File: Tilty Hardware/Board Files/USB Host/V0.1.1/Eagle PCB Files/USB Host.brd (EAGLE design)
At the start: 38.1 x 50.8 mm, 24 parts, among them U1 MAX3421E, U2 AP7313SOT23R, U3 LM2931

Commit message: A bunch of changes to things.todo after assembling new prototypes
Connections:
- removed net N$27: JP4.P$6
- net INT: now also JP4.P$6
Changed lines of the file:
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@@
 <contactref element="JP4" pad="P$5"/>
-</signal>
-<signal name="N$27">
-<contactref element="JP4" pad="P$6"/>
 </signal>
 <signal name="3V_SCL">
@@
 <wire x1="17.8" y1="18.744" x2="17.8" y2="17.1495" width="0.2032" layer="1"/>
 <wire x1="17.8" y1="17.1495" x2="17.8045" y2="17.145" width="0.2032" layer="1"/>
+<contactref element="JP4" pad="P$6"/>
+<wire x1="17.8" y1="18.744" x2="30.607" y2="36.703" width="0" layer="19" extent="1-1"/>
 </signal>
 <signal name="RST">

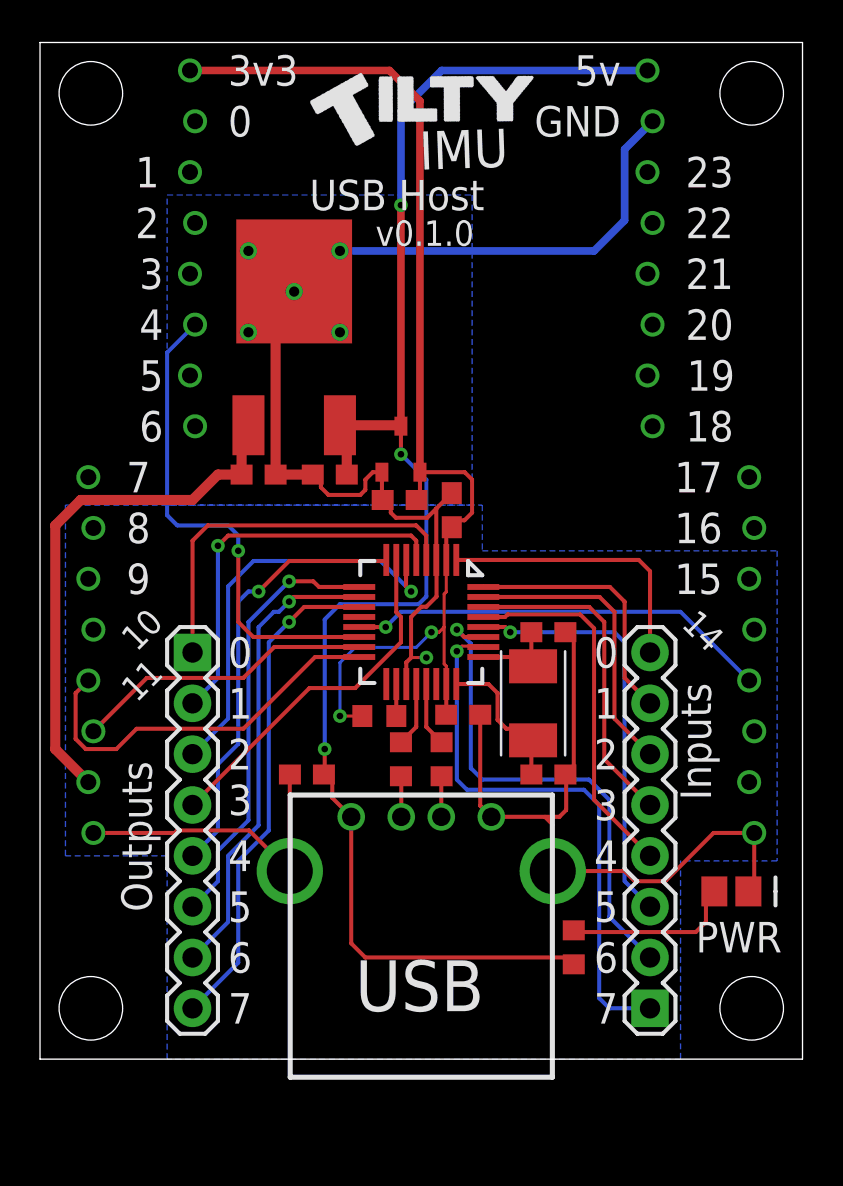
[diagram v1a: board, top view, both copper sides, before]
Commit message: Added Tilty silkscreen and option 5/3.3v I2C connections
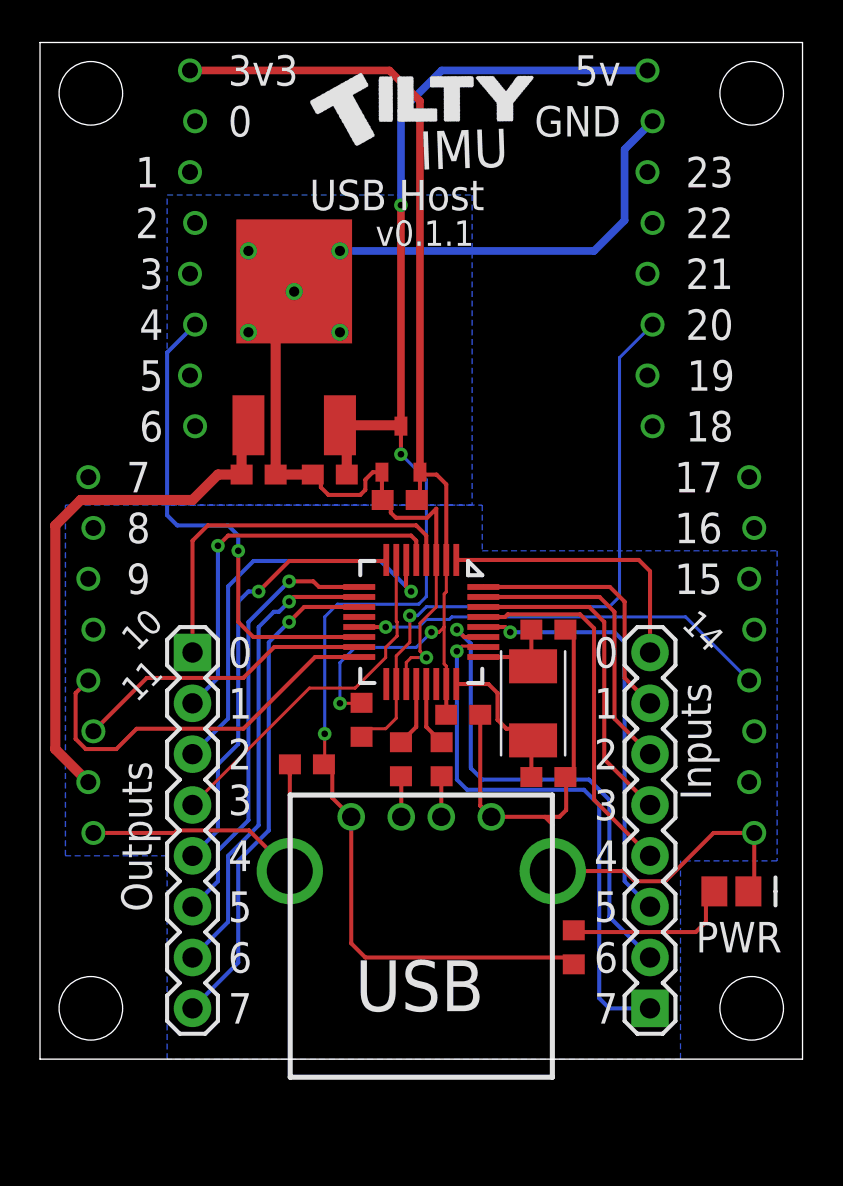
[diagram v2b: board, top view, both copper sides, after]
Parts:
- removed C1: 0.1uF, resistor:C0603
- moved R3 0.91 mm to (16.1, 17.0), turned to 90 degrees
- moved C5 0.51 mm to (13.3, 14.7)
- moved C3 0.13 mm to (25.4, 21.5)
- moved C4 0.13 mm to (25.4, 14.1)
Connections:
- net +3V3: no longer C1.1
- net GND: no longer C1.2
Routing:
- net INT: track 1.60 -> 32.7 mm, vias 0 -> 1
- net +3V3: track 57.2 -> 54.4 mm
- net +5V: track 77.5 -> 78.1 mm
- net GND: track 117.6 -> 117.1 mm
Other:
- board text added: "v0.1.1"
- board text removed: "v0.1.0"

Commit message: Added reset pullup to USB Host add-on
Oops... That should've been there before...
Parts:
- added R5: 10K, resistor:R0603
- R3: value 4.7K -> 10K
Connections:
- net +3V3: now also R5.2
- net RST: now also R5.1
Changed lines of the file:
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@@
 <attribute name="VALUE" x="20.066" y="14.097" size="1.27" layer="27" rot="R90"/>
 </element>
-<element name="R3" library="resistor" package="R0603" value="4.7K" x="16.0655" y="16.9545" smashed="yes" rot="R90">
+<element name="R3" library="resistor" package="R0603" value="10K" x="16.0655" y="16.9545" smashed="yes" rot="R90">
 <attribute name="VALUE" x="18.0975" y="16.0655" size="1.27" layer="27" rot="R90"/>
 </element>
@@
 <attribute name="VALUE" x="28.702" y="4.699" size="1.27" layer="27" rot="R90"/>
 </element>
+<element name="R5" library="resistor" package="R0603" value="10K" x="1.524" y="-3.81"/>
 </elements>
 <signals>
@@
 <wire x1="14.986" y1="17.78" x2="16.041" y2="17.78" width="0.1524" layer="1"/>
 <wire x1="16.041" y1="17.78" x2="16.0655" y2="17.8045" width="0.1524" layer="1"/>
+<contactref element="R5" pad="2"/>
+<wire x1="2.374" y1="-3.81" x2="14.986" y2="17.78" width="0" layer="19" extent="1-16"/>
 </signal>
 <signal name="+5V">
@@
 <signal name="RST">
 <contactref element="U1" pad="12"/>
+<contactref element="R5" pad="1"/>
+<wire x1="0.674" y1="-3.81" x2="15.95" y2="22.094" width="0" layer="19" extent="1-1"/>
 </signal>
 <signal name="N$9">

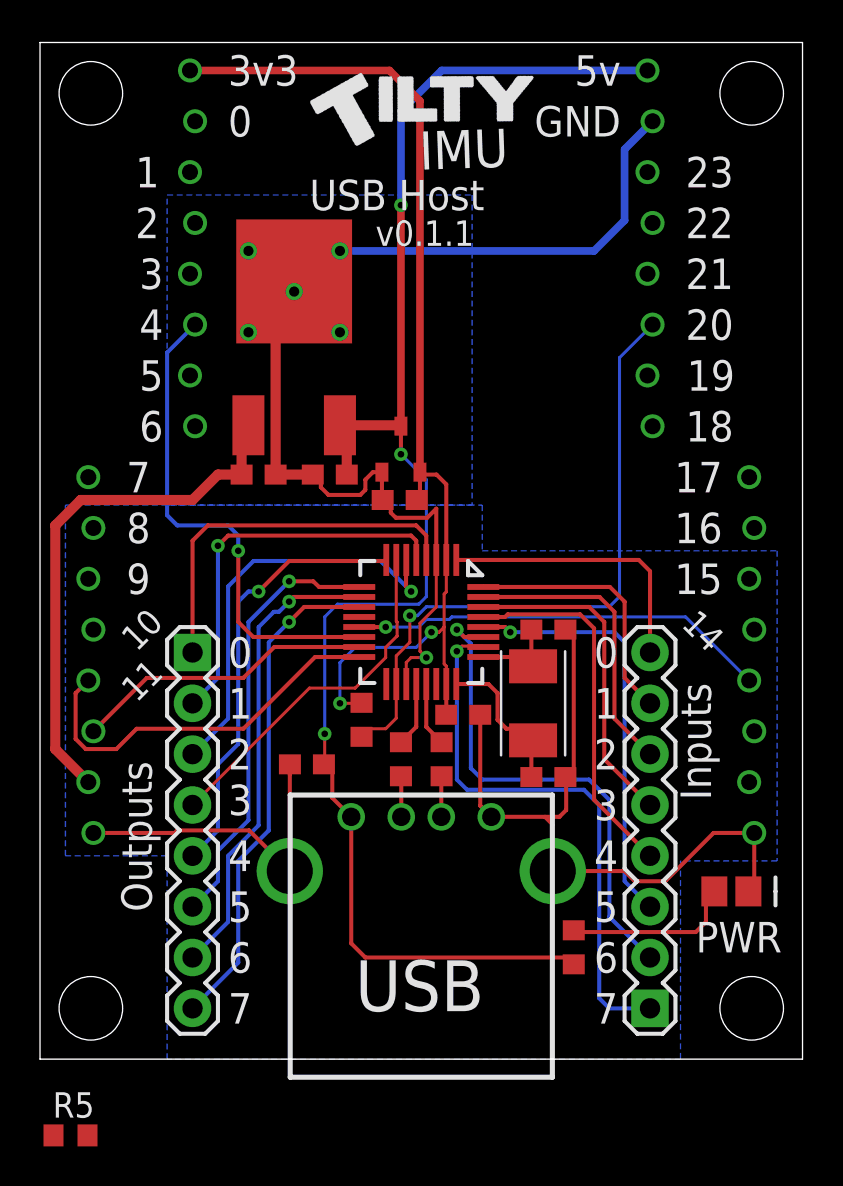
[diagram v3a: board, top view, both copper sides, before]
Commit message: Tweaked some silkscreen labeling
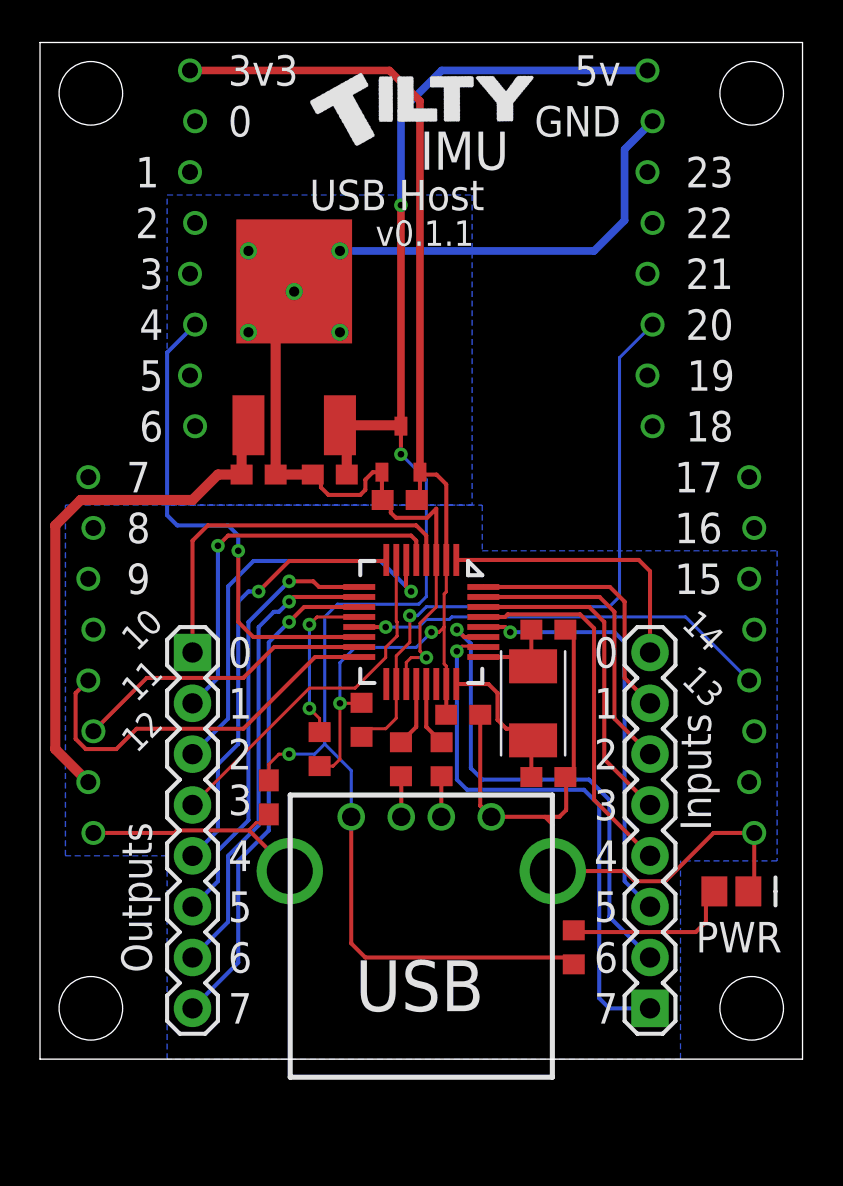
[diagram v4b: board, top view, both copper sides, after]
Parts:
- moved R5 23.0 mm to (14.0, 15.5), turned to 270 degrees
- moved C5 2.52 mm to (11.4, 13.1), turned to 270 degrees
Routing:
- net RST: track 0.00 -> 8.23 mm, vias 0 -> 2
- net GND: track 117.1 -> 113.1 mm
- net +3V3: track 54.4 -> 58.3 mm
- net +5V: track 78.1 -> 81.5 mm
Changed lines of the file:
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@@
 <rectangle x1="24.548215625" y1="49.09040625" x2="24.670134375" y2="49.110725" layer="25" rot="R327"/>
 <rectangle x1="24.6015625" y1="49.112978125" x2="24.62188125" y2="49.133296875" layer="25" rot="R327"/>
-<text x="18.984028125" y="44.441321875" size="1.905" layer="25" font="vector" ratio="17" rot="R2">IMU</text>
+<text x="18.984028125" y="44.441321875" size="1.905" layer="25" font="vector" ratio="17">IMU</text>
 <text x="13.462" y="42.418" size="1.524" layer="25" ratio="12">USB Host</text>
 <text x="16.764" y="40.64" size="1.27" layer="25" ratio="12">v0.1.1</text>
-<text x="5.588" y="7.366" size="1.524" layer="25" ratio="15" rot="R90">Outputs</text>
-<text x="32.004" y="18.796" size="1.524" layer="25" ratio="15" rot="R270">Inputs</text>
+<text x="5.588" y="4.318" size="1.524" layer="25" ratio="15" rot="R90">Outputs</text>
+<text x="32.004" y="17.272" size="1.524" layer="25" ratio="15" rot="R270">Inputs</text>
 <text x="9.398" y="19.558" size="1.524" layer="25" ratio="15">0</text>
 <text x="9.398" y="17.018" size="1.524" layer="25" ratio="15">1</text>
@@
 <text x="31.623" y="18.161" size="1.524" layer="26" ratio="12" rot="MR0" align="bottom-right">13</text>
 <text x="36.449" y="6.4135" size="1.524" layer="26" ratio="12" rot="MR270" align="bottom-right">GND</text>
+<text x="33.401" y="17.4625" size="1.27" layer="25" ratio="15" rot="R315" align="bottom-right">13</text>
+<text x="4.826" y="15.24" size="1.27" layer="25" ratio="15" rot="R45">12</text>
 </plain>
 <attributes>
@@
 <attribute name="VALUE" x="26.289" y="16.129" size="1.27" layer="27" rot="R180"/>
 </element>
-<element name="C5" library="resistor" package="C0603" value="4.7uF" x="13.335" y="14.732" smashed="yes" rot="R180">
-<attribute name="VALUE" x="14.224" y="16.764" size="1.27" layer="27" rot="R180"/>
+<element name="C5" library="resistor" package="C0603" value="4.7uF" x="11.43" y="13.081" smashed="yes" rot="R270">
+<attribute name="VALUE" x="9.398" y="13.97" size="1.27" layer="27" rot="R270"/>
 </element>
 <element name="U2" library="My Parts" package="SOT23" value="AP7313SOT23R" x="18.034" y="30.48" smashed="yes"/>
@@
 <attribute name="VALUE" x="28.702" y="4.699" size="1.27" layer="27" rot="R90"/>
 </element>
-<element name="R5" library="resistor" package="R0603" value="10K" x="1.524" y="-3.81"/>
+<element name="R5" library="resistor" package="R0603" value="10K" x="13.97" y="15.494" smashed="yes" rot="R270">
+<attribute name="VALUE" x="11.938" y="16.383" size="1.27" layer="27" rot="R270"/>
+</element>
 </elements>
 <signals>
@@
 <contactref element="C5" pad="2"/>
 <wire x1="19.8" y1="24.944" x2="19.8" y2="27.508" width="0.2032" layer="1"/>
-<wire x1="12.48" y1="9.398" x2="12.48" y2="14.219" width="0.2032" layer="1"/>
-<wire x1="12.48" y1="14.219" x2="12.485" y2="14.732" width="0.2032" layer="1"/>
 <wire x1="21.9955" y1="17.2085" x2="21.9955" y2="12.6625" width="0.2032" layer="1"/>
 <wire x1="21.9955" y1="12.6625" x2="22.55" y2="12.108" width="0.2032" layer="1"/>
@@
 <wire x1="18.9865" y1="21.7805" x2="18.9865" y2="20.3835" width="0.1524" layer="1"/>
 <wire x1="18.9865" y1="20.3835" x2="19.304" y2="20.066" width="0.1524" layer="1"/>
+<wire x1="10.448" y1="11.43" x2="10.448" y2="11.464" width="0.1524" layer="1"/>
+<wire x1="10.448" y1="11.464" x2="10.795" y2="11.811" width="0.1524" layer="1"/>
+<wire x1="10.795" y1="11.811" x2="11.01" y2="11.811" width="0.1524" layer="1"/>
+<wire x1="11.01" y1="11.811" x2="11.43" y2="12.231" width="0.1524" layer="1"/>
 </signal>
 <signal name="MISO">
@@
 <wire x1="16.041" y1="17.78" x2="16.0655" y2="17.8045" width="0.1524" layer="1"/>
 <contactref element="R5" pad="2"/>
-<wire x1="2.374" y1="-3.81" x2="14.986" y2="17.78" width="0" layer="19" extent="1-16"/>
+<wire x1="13.97" y1="14.644" x2="14.644" y2="14.644" width="0.1524" layer="1"/>
+<wire x1="14.644" y1="14.644" x2="14.986" y2="14.986" width="0.1524" layer="1"/>
+<wire x1="14.986" y1="14.986" x2="14.986" y2="17.78" width="0.1524" layer="1"/>
 </signal>
 <signal name="+5V">
@@
 <contactref element="C8" pad="1"/>
 <contactref element="U2" pad="P$3"/>
-<wire x1="14.185" y1="14.732" x2="14.224" y2="14.478" width="0.2032" layer="1"/>
-<wire x1="14.224" y1="14.478" x2="14.605" y2="14.351" width="0.2032" layer="1"/>
-<wire x1="14.605" y1="14.351" x2="14.605" y2="13.053" width="0.2032" layer="1"/>
-<wire x1="14.605" y1="13.053" x2="15.55" y2="12.108" width="0.2032" layer="1"/>
 <wire x1="15.328" y1="29.21" x2="15.328" y2="31.3318" width="0.508" layer="1"/>
 <wire x1="15.328" y1="31.3318" x2="14.986" y2="31.6738" width="0.508" layer="1"/>
@@
 <wire x1="18.034" y1="47.371" x2="20.066" y2="49.403" width="0.381" layer="16"/>
 <wire x1="20.066" y1="49.403" x2="30.353" y2="49.403" width="0.381" layer="16"/>
-<via x="14.224" y="16.256" extent="1-16" drill="0.3302"/>
-<wire x1="14.224" y1="14.517" x2="14.185" y2="14.732" width="0.2032" layer="1"/>
+<via x="12.446" y="15.24" extent="1-16" drill="0.3302"/>
 <via x="18.034" y="30.226" extent="1-16" drill="0.3302"/>
 <wire x1="18.034" y1="30.226" x2="18.034" y2="31.63" width="0.2032" layer="1"/>
@@
 <wire x1="19.304" y1="28.956" x2="18.034" y2="30.226" width="0.1524" layer="16"/>
 <wire x1="14.859" y1="22.733" x2="14.224" y2="22.098" width="0.1524" layer="16"/>
-<wire x1="14.224" y1="22.098" x2="14.224" y2="16.256" width="0.1524" layer="16"/>
-<wire x1="14.224" y1="16.256" x2="14.224" y2="14.517" width="0.1524" layer="1"/>
-<wire x1="14.224" y1="14.478" x2="14.224" y2="14.517" width="0.1524" layer="1"/>
+<wire x1="14.224" y1="22.098" x2="14.224" y2="15.748" width="0.1524" layer="16"/>
+<wire x1="14.224" y1="15.748" x2="13.716" y2="15.24" width="0.1524" layer="16"/>
+<wire x1="13.716" y1="15.24" x2="12.446" y2="15.24" width="0.1524" layer="16"/>
+<wire x1="15.55" y1="12.108" x2="15.55" y2="14.422" width="0.1524" layer="16"/>
+<wire x1="15.55" y1="14.422" x2="14.224" y2="15.748" width="0.1524" layer="16"/>
+<wire x1="12.446" y1="15.24" x2="11.938" y2="15.24" width="0.1524" layer="1"/>
+<wire x1="11.938" y1="15.24" x2="11.43" y2="14.732" width="0.1524" layer="1"/>
+<wire x1="11.43" y1="14.732" x2="11.43" y2="13.931" width="0.1524" layer="1"/>
 </signal>
 <signal name="VCC">
@@
 <contactref element="U1" pad="12"/>
 <contactref element="R5" pad="1"/>
-<wire x1="0.674" y1="-3.81" x2="15.95" y2="22.094" width="0" layer="19" extent="1-1"/>
+<via x="13.462" y="21.717" extent="1-16" drill="0.3302"/>
+<via x="13.462" y="17.526" extent="1-16" drill="0.3302"/>
+<wire x1="15.95" y1="22.094" x2="13.839" y2="22.094" width="0.1524" layer="1"/>
+<wire x1="13.839" y1="22.094" x2="13.462" y2="21.717" width="0.1524" layer="1"/>
+<wire x1="13.462" y1="21.717" x2="13.462" y2="17.526" width="0.1524" layer="16"/>
+<wire x1="13.462" y1="17.526" x2="13.97" y2="17.018" width="0.1524" layer="1"/>
+<wire x1="13.97" y1="17.018" x2="13.97" y2="16.344" width="0.1524" layer="1"/>
 </signal>
 <signal name="N$9">
